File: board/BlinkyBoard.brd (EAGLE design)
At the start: 33 x 12.2 mm, 18 parts, among them Q1 16 MHz

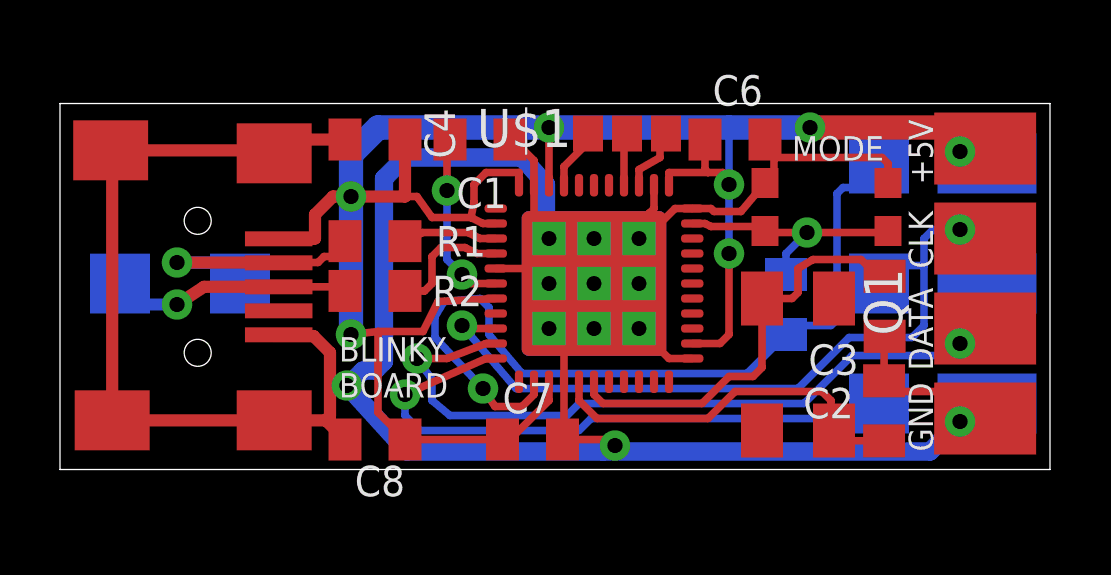
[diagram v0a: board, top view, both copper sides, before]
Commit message: Snap dimensions to inches
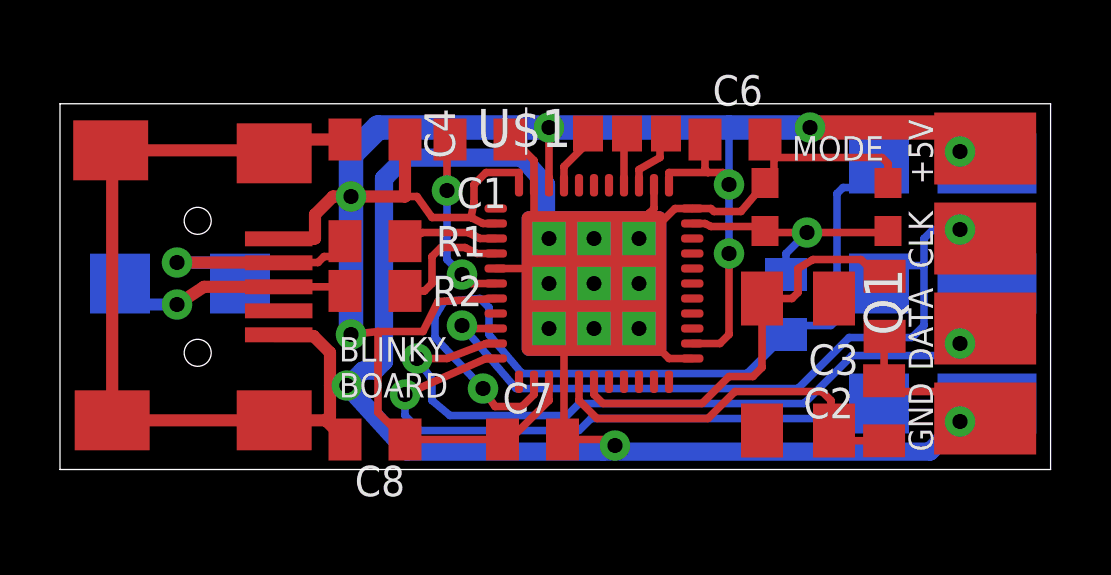
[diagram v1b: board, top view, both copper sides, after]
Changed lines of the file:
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@@
 <setting verticaltext="up"/>
 </settings>
-<grid distance="0.1" unitdist="inch" unit="inch" style="lines" multiple="1" display="yes" altdistance="0.1" altunitdist="mm" altunit="mm"/>
+<grid distance="0.01" unitdist="inch" unit="inch" style="lines" multiple="1" display="yes" altdistance="0.1" altunitdist="mm" altunit="mm"/>
 <layers>
 <layer number="1" name="Top" color="4" fill="1" visible="yes" active="yes"/>
@@
 <layer number="27" name="tValues" color="7" fill="1" visible="no" active="yes"/>
 <layer number="28" name="bValues" color="7" fill="1" visible="no" active="yes"/>
-<layer number="29" name="tStop" color="7" fill="3" visible="no" active="yes"/>
-<layer number="30" name="bStop" color="7" fill="6" visible="no" active="yes"/>
+<layer number="29" name="tStop" color="7" fill="3" visible="yes" active="yes"/>
+<layer number="30" name="bStop" color="7" fill="6" visible="yes" active="yes"/>
 <layer number="31" name="tCream" color="7" fill="4" visible="no" active="yes"/>
 <layer number="32" name="bCream" color="7" fill="5" visible="no" active="yes"/>
@@
 <board>
 <plain>
-<wire x1="0" y1="0" x2="0" y2="12.2" width="0" layer="20"/>
-<wire x1="0" y1="12.2" x2="33" y2="12.2" width="0" layer="20"/>
-<wire x1="0" y1="0" x2="33" y2="0" width="0" layer="20"/>
-<wire x1="33" y1="12.2" x2="33" y2="0" width="0" layer="20"/>
+<wire x1="0" y1="0" x2="0" y2="12.192" width="0" layer="20"/>
+<wire x1="0" y1="12.192" x2="33.02" y2="12.192" width="0" layer="20"/>
+<wire x1="0" y1="0" x2="33.02" y2="0" width="0" layer="20"/>
+<wire x1="33.02" y1="12.192" x2="33.02" y2="0" width="0" layer="20"/>
 <rectangle x1="1.3843" y1="0.3683" x2="14.2621" y2="0.3937" layer="22" rot="R180"/>
 <rectangle x1="1.3843" y1="0.3937" x2="14.2621" y2="0.4191" layer="22" rot="R180"/>
